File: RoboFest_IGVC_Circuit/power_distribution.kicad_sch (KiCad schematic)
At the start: 9 parts, among them J1 Conn_01x02, J2 Conn_01x03, J3 Conn_01x02, J4 Conn_01x03, J5 Conn_01x03, J6 Conn_01x03, J7 Conn_01x03

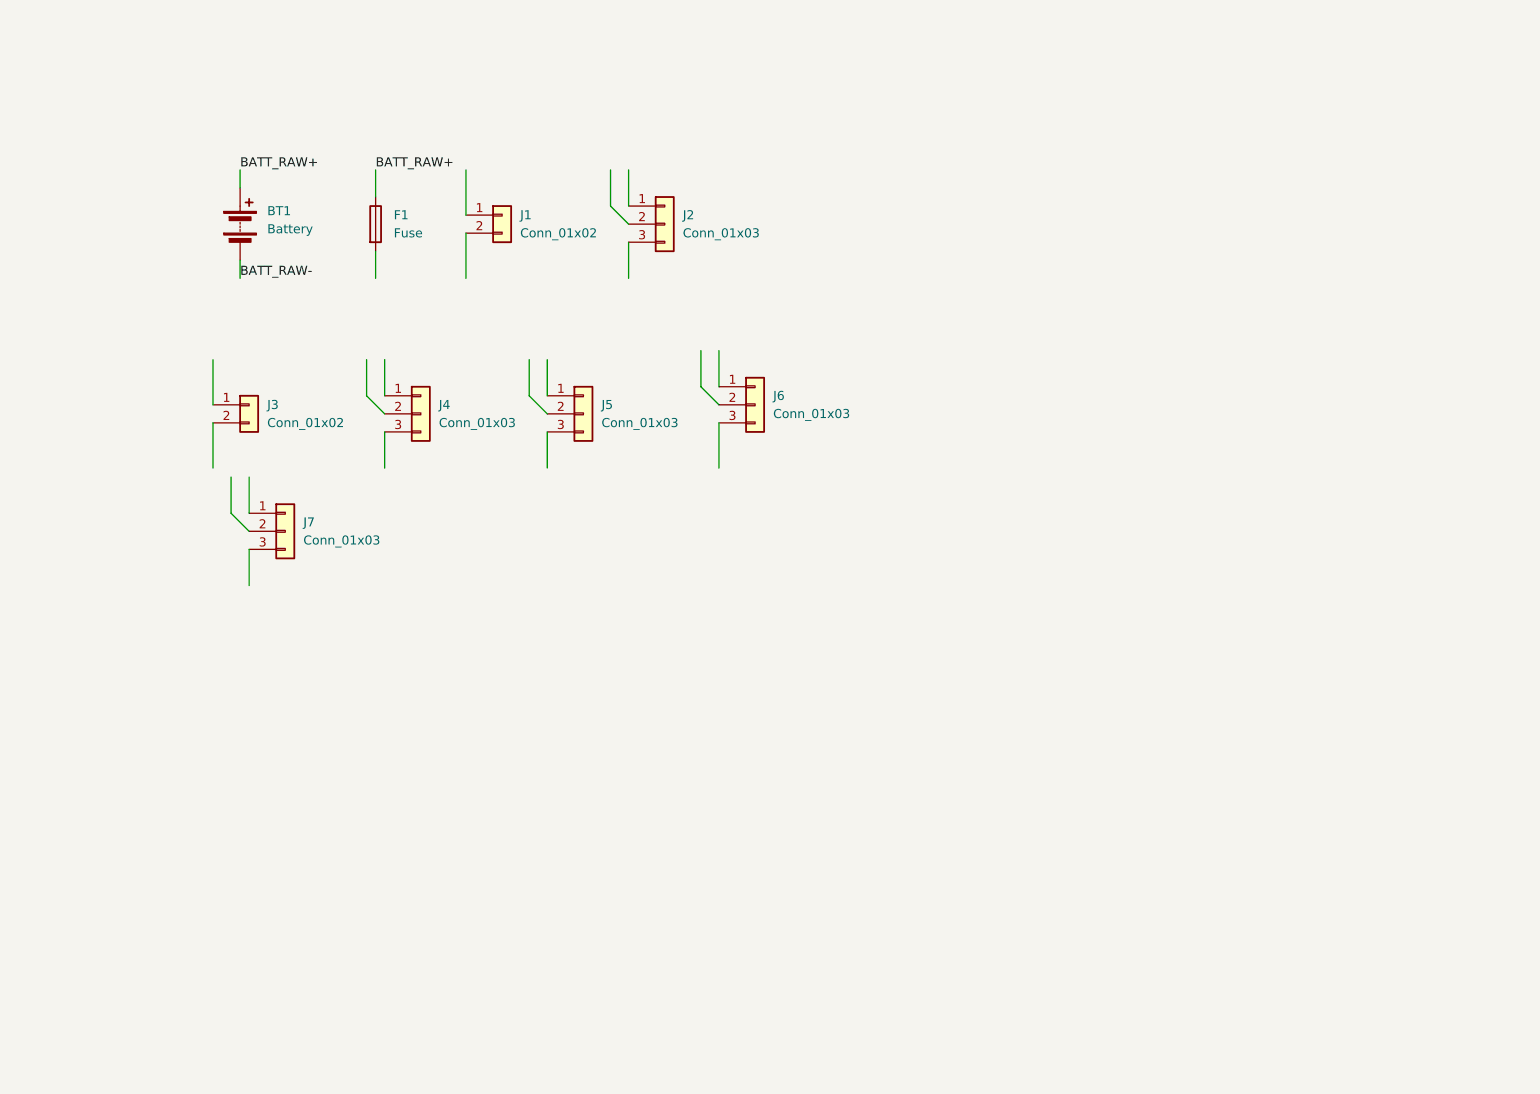
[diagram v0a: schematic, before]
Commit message: added STM32 pinout and report and code
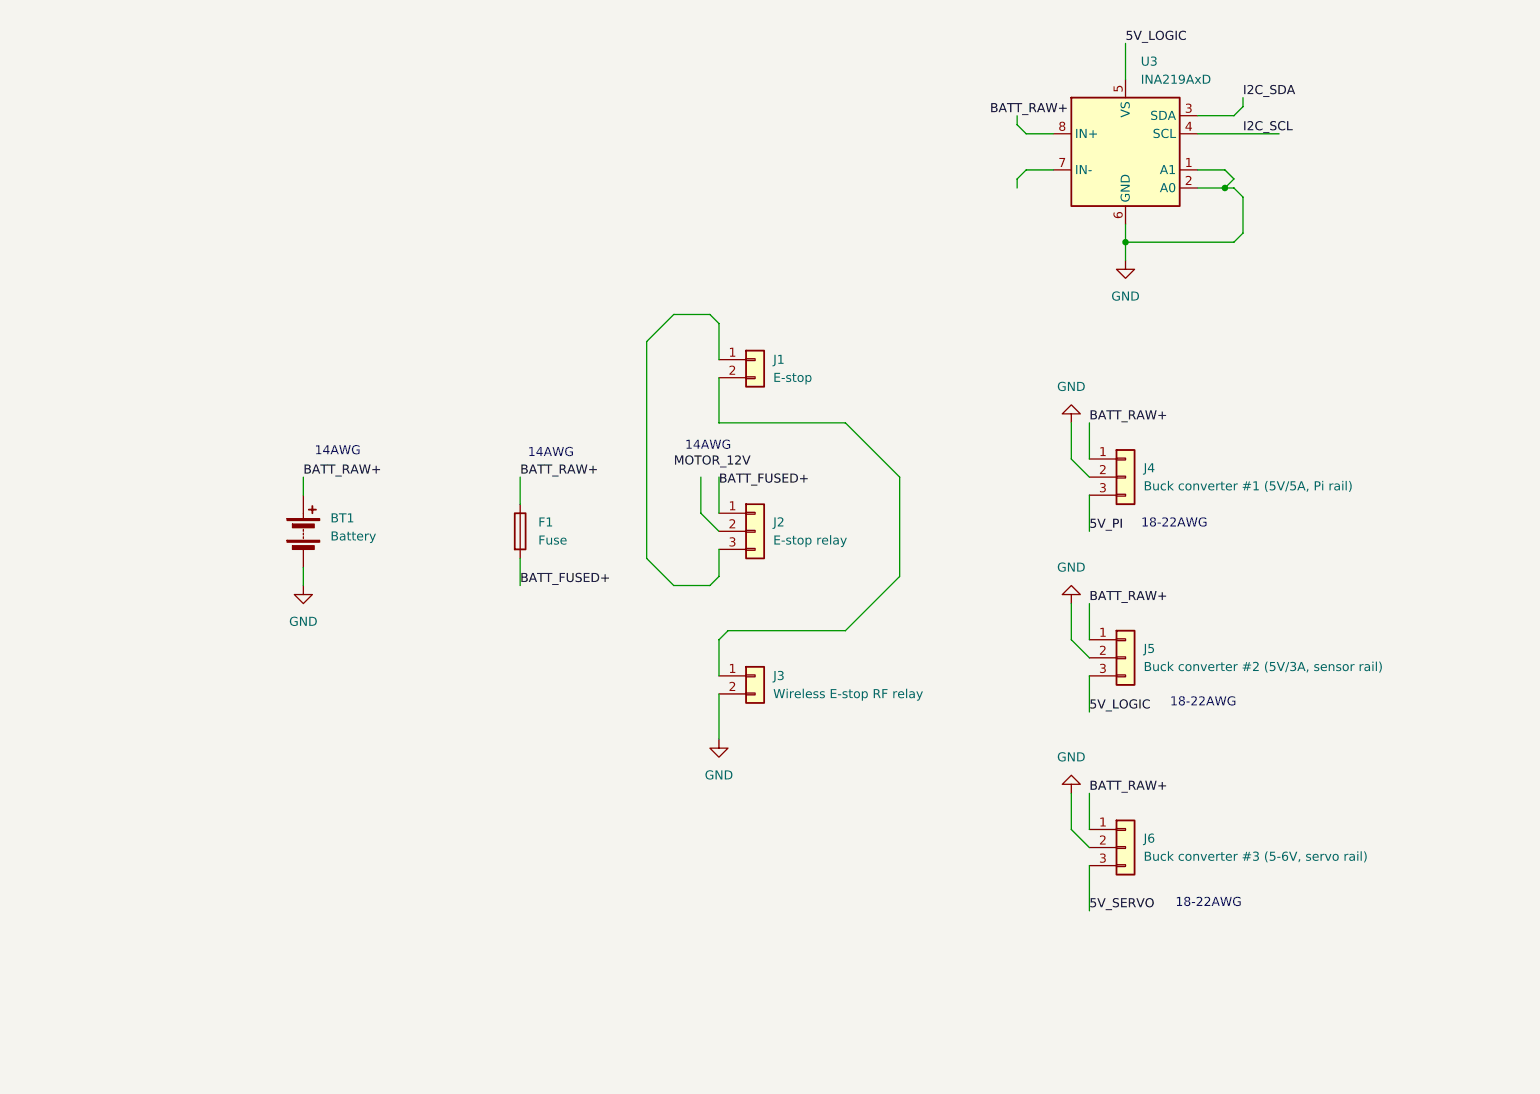
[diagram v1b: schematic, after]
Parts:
- removed J7: Conn_01x03, symbol Connector_Generic:Conn_01x03
- added U3: INA219AxD, Package_SO:SOIC-8_3.9x4.9mm_P1.27mm, symbol Sensor_Energy:INA219AxD
- J1: value Conn_01x02 -> E-stop
- J2: value Conn_01x03 -> E-stop relay
- J3: value Conn_01x02 -> Wireless E-stop RF relay
- J4: value Conn_01x03 -> Buck converter #1 (5V/5A, Pi rail)
- J5: value Conn_01x03 -> Buck converter #2 (5V/3A, sensor rail)
- J6: value Conn_01x03 -> Buck converter #3 (5-6V, servo rail)
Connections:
- net BATT_RAW- is gone; now on net GND: BT1.2 (-)
- net BATT_RAW+: now also J4.1 (Pin_1), J5.1 (Pin_1), J6.1 (Pin_1)
- net at J1.1 (Pin_1): now also J2.3 (Pin_3)
- net at J1.2 (Pin_2): now also J3.1 (Pin_1)
- net GND: now reaches J5.2 (Pin_2)
- net GND: now also J3.2 (Pin_2), J4.2 (Pin_2), J6.2 (Pin_2), U3.1 (A1), U3.2 (A0), U3.6 (GND)
- net 5V_LOGIC: now reaches J5.3 (Pin_3)
- net 5V_LOGIC: now also U3.5 (VS)
- net 5V_SERVO: now reaches J6.3 (Pin_3)
- net BATT_FUSED+: now reaches J2.1 (Pin_1)
- net BATT_FUSED+: now also F1.2
- net 5V_PI: now reaches J4.3 (Pin_3)
- new net I2C_SCL: U3.4 (SCL)
- new net I2C_SDA: U3.3 (SDA)
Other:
- note added: "14AWG"
- note added: "18-22AWG"
- moved on the sheet: BT1, F1, J1, J2, J3, J4, J5, J6

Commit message: updated diagram
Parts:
- added U5: INA219AxD, Package_SO:SOIC-8_3.9x4.9mm_P1.27mm, symbol Sensor_Energy:INA219AxD
- BT1: value Battery -> 3S LiPo (11.1-12.6V)
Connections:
- net 5V_LOGIC: now also U5.2 (A0), U5.5 (VS)
- net 5V_PI: now also U5.7 (IN-); no longer J4.3 (Pin_3)
- net BATT_FUSED+: now also U3.8 (IN+)
- net BATT_RAW+: no longer F1.1, J4.1 (Pin_1), J5.1 (Pin_1), J6.1 (Pin_1)
- net GND: now also U5.1 (A1), U5.6 (GND)
- net I2C_SCL: now also U5.4 (SCL)
- net I2C_SDA: now also U5.3 (SDA)
- net MOTOR_12V: now also J2.2 (Pin_2)
- net BATT_SENSED+: now reaches U3.7 (IN-)
- net BATT_SENSED+: now also F1.1, J4.1 (Pin_1), J5.1 (Pin_1), J6.1 (Pin_1)
- new net BUCK1_OUT_RAW: J4.3 (Pin_3), U5.8 (IN+)
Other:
- note added: "0x40"
- note added: "0x41"
- note added: "BATT Current Sensor"
- note added: "Battery Unit"
- note added: "Buck Convertor Unit"
- note added: "Current Sensor Unit"
- note added: "Emergency Stop Unit"
- note added: "PI_5 Current Sensor"
- moved on the sheet: BT1, F1, J1, J2, J3, J4, J5, J6, U3

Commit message: updated diagram
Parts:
- added OC1: PC817, PCM_Package_DIP_AKL:DIP-4_W7.62mm_LongPads, symbol PCM_Optocoupler_AKL:PC817
- added R1: 1k, symbol Device:R
- added R2: 10k, symbol Device:R
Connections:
- net BATT_FUSED+: now also R1.1
- net BATT_RAW+: now also F1.1
- net BATT_SENSED+: no longer F1.1
- net GND: now also OC1.3
- net at J1.1 (Pin_1), J2.3 (Pin_3): now also OC1.2
- new net: OC1.1, R1.2
- new net 3V3: R2.2
- new net ESTOP_SENSE: OC1.4, R2.1
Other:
- moved on the sheet: J1, J2, J3
